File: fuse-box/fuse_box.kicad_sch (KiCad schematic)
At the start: 43 parts, among them J1 PWR, J3 Conn_02x05_Counter_Clockwise, U1 AP63200WU

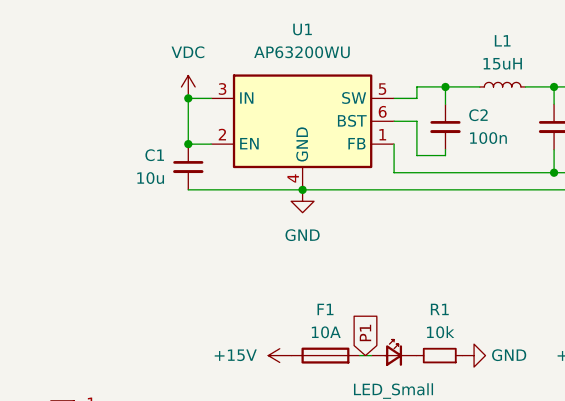
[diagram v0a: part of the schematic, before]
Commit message: feat: improve buck feedback
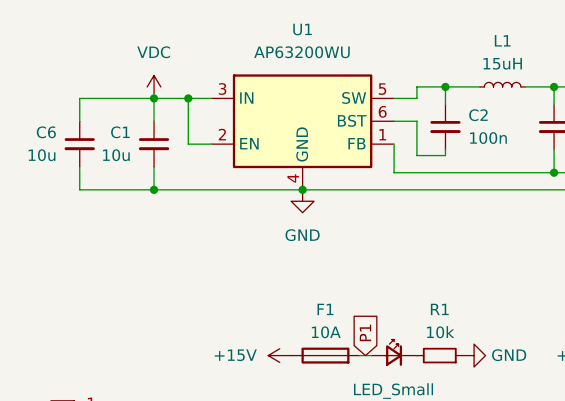
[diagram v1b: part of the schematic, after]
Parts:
- added C6: 10u, Capacitor_SMD:C_0805_2012Metric, symbol Device:C_Small
- L1: footprint Inductor_SMD:L_Bourns_SRP1050WA -> Inductor_SMD:L_Coilcraft_XAL6060-XXX
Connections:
- net GND: now also C6.2
- net VDC: now also C6.1
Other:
- moved on the sheet: C1
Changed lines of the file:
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@@
   (junction (at 97.155 38.1) (diameter 0) (color 0 0 0 0)
   )
+  (junction (at 31.75 38.1) (diameter 0) (color 0 0 0 0)
+  )
+  (junction (at 31.75 27.94) (diameter 0) (color 0 0 0 0)
+  )
   (junction (at 106.045 26.67) (diameter 0) (color 0 0 0 0)
   )
@@
   (junction (at 87.63 38.1) (diameter 0) (color 0 0 0 0)
   )
-  (junction (at 35.56 33.02) (diameter 0) (color 0 0 0 0)
-  )
   (junction (at 97.155 26.67) (diameter 0) (color 0 0 0 0)
   )
@@
     (stroke (width 0) (type default))
   )
+  (wire (pts (xy 31.75 27.94) (xy 35.56 27.94))
+    (stroke (width 0) (type default))
+  )
+  (wire (pts (xy 23.495 38.1) (xy 31.75 38.1))
+    (stroke (width 0) (type default))
+  )
   (wire (pts (xy 83.82 36.195) (xy 83.82 32.385))
     (stroke (width 0) (type default))
@@
     (stroke (width 0) (type default))
   )
+  (wire (pts (xy 23.495 27.94) (xy 23.495 30.48))
+    (stroke (width 0) (type default))
+  )
   (wire (pts (xy 54.61 88.9) (xy 55.88 88.9))
     (stroke (width 0) (type default))
   )
-  (wire (pts (xy 35.56 38.1) (xy 48.26 38.1))
+  (wire (pts (xy 23.495 35.56) (xy 23.495 38.1))
     (stroke (width 0) (type default))
   )
@@
     (stroke (width 0) (type default))
   )
+  (wire (pts (xy 31.75 35.56) (xy 31.75 38.1))
+    (stroke (width 0) (type default))
+  )
   (wire (pts (xy 60.96 26.67) (xy 60.96 27.94))
     (stroke (width 0) (type default))
@@
     (stroke (width 0) (type default))
   )
+  (wire (pts (xy 31.75 27.94) (xy 31.75 30.48))
+    (stroke (width 0) (type default))
+  )
   (wire (pts (xy 73.025 26.67) (xy 76.2 26.67))
     (stroke (width 0) (type default))
@@
     (stroke (width 0) (type default))
   )
-  (wire (pts (xy 35.56 33.02) (xy 35.56 27.94))
-    (stroke (width 0) (type default))
-  )
   (wire (pts (xy 87.63 38.1) (xy 48.26 38.1))
     (stroke (width 0) (type default))
@@
     (stroke (width 0) (type default))
   )
+  (wire (pts (xy 31.75 38.1) (xy 48.26 38.1))
+    (stroke (width 0) (type default))
+  )
   (wire (pts (xy 35.56 27.94) (xy 38.1 27.94))
     (stroke (width 0) (type default))
@@
     (stroke (width 0) (type default))
   )
+  (wire (pts (xy 23.495 27.94) (xy 31.75 27.94))
+    (stroke (width 0) (type default))
+  )
   (wire (pts (xy 60.96 26.67) (xy 64.135 26.67))
     (stroke (width 0) (type default))
@@
   )
   (wire (pts (xy 60.96 27.94) (xy 58.42 27.94))
+    (stroke (width 0) (type default))
+  )
+  (wire (pts (xy 35.56 27.94) (xy 35.56 33.02))
     (stroke (width 0) (type default))
   )
@@
       (effects (font (size 1.27 1.27)))
     )
-    (property "Footprint" "Inductor_SMD:L_Bourns_SRP1050WA" (at 70.485 26.67 0)
+    (property "Footprint" "Inductor_SMD:L_Coilcraft_XAL6060-XXX" (at 70.485 26.67 0)
       (effects (font (size 1.27 1.27)) hide)
     )
@@
     )
   )
-  (symbol (lib_id "power:VDC") (at 35.56 27.94 0) (unit 1)
-    (in_bom yes) (on_board yes) (dnp no) (fields_autoplaced)
-    (property "Reference" "#PWR032" (at 35.56 30.48 0)
-      (effects (font (size 1.27 1.27)) hide)
-    )
-    (property "Value" "VDC" (at 35.56 22.86 0)
-      (effects (font (size 1.27 1.27)))
-    )
-    (property "Footprint" "" (at 35.56 27.94 0)
-      (effects (font (size 1.27 1.27)) hide)
-    )
-    (property "Datasheet" "" (at 35.56 27.94 0)
+  (symbol (lib_id "Device:C_Small") (at 23.495 33.02 0) (mirror y) (unit 1)
+    (in_bom yes) (on_board yes) (dnp no)
+    (property "Reference" "C6" (at 20.955 31.7563 0)
+      (effects (font (size 1.27 1.27)) (justify left))
+    )
+    (property "Value" "10u" (at 20.955 34.2963 0)
+      (effects (font (size 1.27 1.27)) (justify left))
+    )
+    (property "Footprint" "Capacitor_SMD:C_0805_2012Metric" (at 23.495 33.02 0)
+      (effects (font (size 1.27 1.27)) hide)
+    )
+    (property "Datasheet" "~" (at 23.495 33.02 0)
+      (effects (font (size 1.27 1.27)) hide)
+    )
+    (pin "1")
+    (pin "2")
+    (instances
+      (project "fuse_box"
+        (path "/f3a05ee0-841f-4a07-a027-0a71a1b51dd2"
+          (reference "C6") (unit 1)
+        )
+      )
+    )
+  )
+  (symbol (lib_id "power:VDC") (at 31.75 27.94 0) (unit 1)
+    (in_bom yes) (on_board yes) (dnp no) (fields_autoplaced)
+    (property "Reference" "#PWR032" (at 31.75 30.48 0)
+      (effects (font (size 1.27 1.27)) hide)
+    )
+    (property "Value" "VDC" (at 31.75 22.86 0)
+      (effects (font (size 1.27 1.27)))
+    )
+    (property "Footprint" "" (at 31.75 27.94 0)
+      (effects (font (size 1.27 1.27)) hide)
+    )
+    (property "Datasheet" "" (at 31.75 27.94 0)
       (effects (font (size 1.27 1.27)) hide)
     )
@@
     )
   )
-  (symbol (lib_id "Device:C_Small") (at 35.56 35.56 0) (mirror y) (unit 1)
-    (in_bom yes) (on_board yes) (dnp no)
-    (property "Reference" "C1" (at 33.02 34.2963 0)
-      (effects (font (size 1.27 1.27)) (justify left))
-    )
-    (property "Value" "10u" (at 33.02 36.8363 0)
-      (effects (font (size 1.27 1.27)) (justify left))
-    )
-    (property "Footprint" "Capacitor_SMD:C_0805_2012Metric" (at 35.56 35.56 0)
-      (effects (font (size 1.27 1.27)) hide)
-    )
-    (property "Datasheet" "~" (at 35.56 35.56 0)
-      (effects (font (size 1.27 1.27)) hide)
-    )
+  (symbol (lib_id "Device:C_Small") (at 31.75 33.02 0) (mirror y) (unit 1)
+    (in_bom yes) (on_board yes) (dnp no)
+    (property "Reference" "C1" (at 29.21 31.7563 0)
+      (effects (font (size 1.27 1.27)) (justify left))
+    )
+    (property "Value" "10u" (at 29.21 34.2963 0)
+      (effects (font (size 1.27 1.27)) (justify left))
+    )
+    (property "Footprint" "Capacitor_SMD:C_0805_2012Metric" (at 31.75 33.02 0)
+      (effects (font (size 1.27 1.27)) hide)
+    )
+    (property "Datasheet" "~" (at 31.75 33.02 0)
+      (effects (font (size 1.27 1.27)) hide)
+    )

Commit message: Add files via upload
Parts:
- removed F1, F2, F3, F4, F5, F6, F7, F8, F9: 10A, PCM_Fuse_AKL:Fuseholder_Blade_ATO_Littelfuse_Pudenz_2_Pin, symbol Device:Fuse
- added F1, F2, F3, F4, F5, F6, F7, F8, F9: 178.6164.0001, fuseholder:LITTELFUSE_178.6164.0001, symbol 178.6164.0001:178.6164.0001
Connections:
- net +15V: now also F1.1, F2.1, F3.1, F4.1, F5.1, F6.1, F7.1, F8.1, F9.1
- net P1: now also F1.2
- net P2: now also F2.2
- net P3: now also F3.2
- net P4: now also F4.2
- net P5: now also F5.2
- net P6: now also F6.2
- net P7: now also F7.2
- net P8: now also F8.2
- net P9: now also F9.2
